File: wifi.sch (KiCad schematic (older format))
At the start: 70 parts

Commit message: gpio assignment done
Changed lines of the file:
@@
 $Descr A4 11693 8268
 encoding utf-8
-Sheet 9 10
+Sheet 8 10
 Title ""
 Date ""
@@
 $EndComp
 Wire Wire Line
-	2950 3825 2950 3925
+	2950 3825 2950 3875
+Wire Wire Line
+	2950 3875 2950 3925
 Wire Wire Line
 	2950 3925 3000 3925
@@
 $EndComp
 Wire Wire Line
-	4300 3825 4300 3925
+	4300 3825 4300 3875
+Wire Wire Line
+	4300 3875 4300 3925
 Wire Wire Line
 	4300 3925 4200 3925
@@
 	1200 4825 2025 4825
 Wire Wire Line
-	2325 4825 3000 4825
+	2325 4825 2425 4825
+Wire Wire Line
+	2425 4825 3000 4825
 Wire Wire Line
 	2425 4875 2425 4825
@@
 	1100 4525 3000 4525
 Wire Wire Line
-	1100 3425 1100 3625
-Wire Wire Line
-	1100 3475 1725 3475
+	1100 3425 1100 3475
+Wire Wire Line
+	1100 3475 1100 3625
+Wire Wire Line
+	1100 3475 1225 3475
+Wire Wire Line
+	1225 3475 1350 3475
+Wire Wire Line
+	1350 3475 1475 3475
+Wire Wire Line
+	1475 3475 1600 3475
+Wire Wire Line
+	1600 3475 1725 3475
 Wire Wire Line
 	1725 3475 1725 3625
@@
 $EndComp
 Wire Wire Line
-	6925 1900 6925 3600
+	6925 1900 6925 2500
+Wire Wire Line
+	6925 2500 6925 2700
+Wire Wire Line
+	6925 2700 6925 3300
+Wire Wire Line
+	6925 3300 6925 3400
+Wire Wire Line
+	6925 3400 6925 3500
+Wire Wire Line
+	6925 3500 6925 3600
 Wire Wire Line
 	6925 1900 7025 1900
@@
 	6825 3100 7025 3100
 Wire Wire Line
-	6825 3200 7025 3200
+	6825 3200 6875 3200
+Wire Wire Line
+	6875 3200 7025 3200
 Text Label 5950 2800 0    60   ~ 0
 WL_SDIO_D0
@@
 $EndComp
 Wire Wire Line
-	2950 5550 2950 5650
+	2950 5550 2950 5600
+Wire Wire Line
+	2950 5600 2950 5650
 Wire Wire Line
 	2950 5650 3000 5650
@@
 $EndComp
 Wire Wire Line
-	4300 5550 4300 5650
+	4300 5550 4300 5600
+Wire Wire Line
+	4300 5600 4300 5650
 Wire Wire Line
 	4300 5650 4200 5650
@@
 	2400 6600 2400 5950
 Wire Wire Line
-	1600 5950 3000 5950
-Wire Wire Line
-	1600 5850 3000 5850
+	1600 5950 2400 5950
+Wire Wire Line
+	2400 5950 3000 5950
+Wire Wire Line
+	1600 5850 2200 5850
+Wire Wire Line
+	2200 5850 3000 5850
 Wire Wire Line
 	2200 5850 2200 6600
@@
 	4400 6600 4400 6350
 Wire Wire Line
-	4200 6350 5750 6350
+	4200 6350 4400 6350
+Wire Wire Line
+	4400 6350 5750 6350
 Wire Wire Line
 	4600 6600 4600 6150
 Wire Wire Line
-	4200 6150 5750 6150
+	4200 6150 4600 6150
+Wire Wire Line
+	4600 6150 5750 6150
 Wire Wire Line
 	4200 5750 5750 5750
@@
 $EndComp
 Wire Wire Line
-	7925 3900 7925 4000
+	7925 3900 7925 3975
+Wire Wire Line
+	7925 3975 7925 4000
 Wire Wire Line
 	8025 3900 8025 3975
 Wire Wire Line
-	7925 3975 9125 3975
+	7925 3975 8025 3975
+Wire Wire Line
+	8025 3975 8325 3975
+Wire Wire Line
+	8325 3975 8425 3975
+Wire Wire Line
+	8425 3975 8825 3975
+Wire Wire Line
+	8825 3975 8925 3975
+Wire Wire Line
+	8925 3975 9025 3975
+Wire Wire Line
+	9025 3975 9125 3975
 Connection ~ 7925 3975
 Wire Wire Line
@@
 $EndComp
 Wire Wire Line
-	9225 3900 9225 4425
+	9225 3900 9225 4400
+Wire Wire Line
+	9225 4400 9225 4425
 $Comp
 L CONN_COAXIAL J?
@@
 	8725 4050 8725 3900
 Wire Wire Line
-	10125 1900 10125 3600
+	10125 1900 10125 2000
+Wire Wire Line
+	10125 2000 10125 2300
+Wire Wire Line
+	10125 2300 10125 2400
+Wire Wire Line
+	10125 2400 10125 2900
+Wire Wire Line
+	10125 2900 10125 3100
+Wire Wire Line
+	10125 3100 10125 3300
+Wire Wire Line
+	10125 3300 10125 3400
+Wire Wire Line
+	10125 3400 10125 3500
+Wire Wire Line
+	10125 3500 10125 3600
 Wire Wire Line
 	10125 1900 10025 1900
@@
 $EndComp
 Wire Wire Line
-	6425 5400 6900 5400
-Wire Wire Line
-	6850 5350 6850 5450
+	6425 5400 6850 5400
+Wire Wire Line
+	6850 5400 6900 5400
+Wire Wire Line
+	6850 5350 6850 5400
+Wire Wire Line
+	6850 5400 6850 5450
 Connection ~ 6850 5400
 $Comp
@@
 	10025 2500 10150 2500
 Wire Wire Line
-	10025 2100 10975 2100
+	10025 2100 10200 2100
+Wire Wire Line
+	10200 2100 10750 2100
+Wire Wire Line
+	10750 2100 10850 2100
+Wire Wire Line
+	10850 2100 10975 2100
 Wire Wire Line
 	10200 2100 10200 2200
@@
 	10850 3000 10850 2950
 Wire Wire Line
-	10025 3000 11000 3000
+	10025 3000 10750 3000
+Wire Wire Line
+	10750 3000 10850 3000
+Wire Wire Line
+	10850 3000 11000 3000
 $Comp
 L C C?
@@
 $EndComp
 Wire Wire Line
-	7750 1400 8825 1400
+	7750 1400 7825 1400
+Wire Wire Line
+	7825 1400 7925 1400
+Wire Wire Line
+	7925 1400 8125 1400
+Wire Wire Line
+	8125 1400 8325 1400
+Wire Wire Line
+	8325 1400 8725 1400
+Wire Wire Line
+	8725 1400 8825 1400
 Wire Wire Line
 	8825 1400 8825 1450

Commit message: gpio connectors
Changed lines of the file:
@@
 $EndComp
 Wire Wire Line
-	2950 3825 2950 3875
-Wire Wire Line
-	2950 3875 2950 3925
+	2950 3825 2950 3925
 Wire Wire Line
 	2950 3925 3000 3925
@@
 $EndComp
 Wire Wire Line
-	4300 3825 4300 3875
-Wire Wire Line
-	4300 3875 4300 3925
+	4300 3825 4300 3925
 Wire Wire Line
 	4300 3925 4200 3925
@@
 	1200 4825 2025 4825
 Wire Wire Line
-	2325 4825 2425 4825
-Wire Wire Line
-	2425 4825 3000 4825
+	2325 4825 3000 4825
 Wire Wire Line
 	2425 4875 2425 4825
@@
 	1100 4525 3000 4525
 Wire Wire Line
-	1100 3425 1100 3475
-Wire Wire Line
-	1100 3475 1100 3625
-Wire Wire Line
-	1100 3475 1225 3475
-Wire Wire Line
-	1225 3475 1350 3475
-Wire Wire Line
-	1350 3475 1475 3475
-Wire Wire Line
-	1475 3475 1600 3475
-Wire Wire Line
-	1600 3475 1725 3475
+	1100 3425 1100 3625
+Wire Wire Line
+	1100 3475 1725 3475
 Wire Wire Line
 	1725 3475 1725 3625
@@
 $EndComp
 Wire Wire Line
-	6925 1900 6925 2500
-Wire Wire Line
-	6925 2500 6925 2700
-Wire Wire Line
-	6925 2700 6925 3300
-Wire Wire Line
-	6925 3300 6925 3400
-Wire Wire Line
-	6925 3400 6925 3500
-Wire Wire Line
-	6925 3500 6925 3600
+	6925 1900 6925 3600
 Wire Wire Line
 	6925 1900 7025 1900
@@
 	6825 3100 7025 3100
 Wire Wire Line
-	6825 3200 6875 3200
-Wire Wire Line
-	6875 3200 7025 3200
+	6825 3200 7025 3200
 Text Label 5950 2800 0    60   ~ 0
 WL_SDIO_D0
@@
 $EndComp
 Wire Wire Line
-	2950 5550 2950 5600
-Wire Wire Line
-	2950 5600 2950 5650
+	2950 5550 2950 5650
 Wire Wire Line
 	2950 5650 3000 5650
@@
 $EndComp
 Wire Wire Line
-	4300 5550 4300 5600
-Wire Wire Line
-	4300 5600 4300 5650
+	4300 5550 4300 5650
 Wire Wire Line
 	4300 5650 4200 5650
@@
 	2400 6600 2400 5950
 Wire Wire Line
-	1600 5950 2400 5950
-Wire Wire Line
-	2400 5950 3000 5950
-Wire Wire Line
-	1600 5850 2200 5850
-Wire Wire Line
-	2200 5850 3000 5850
+	1600 5950 3000 5950
+Wire Wire Line
+	1600 5850 3000 5850
 Wire Wire Line
 	2200 5850 2200 6600
@@
 	4400 6600 4400 6350
 Wire Wire Line
-	4200 6350 4400 6350
-Wire Wire Line
-	4400 6350 5750 6350
+	4200 6350 5750 6350
 Wire Wire Line
 	4600 6600 4600 6150
 Wire Wire Line
-	4200 6150 4600 6150
-Wire Wire Line
-	4600 6150 5750 6150
+	4200 6150 5750 6150
 Wire Wire Line
 	4200 5750 5750 5750
@@
 $EndComp
 Wire Wire Line
-	7925 3900 7925 3975
-Wire Wire Line
-	7925 3975 7925 4000
+	7925 3900 7925 4000
 Wire Wire Line
 	8025 3900 8025 3975
 Wire Wire Line
-	7925 3975 8025 3975
-Wire Wire Line
-	8025 3975 8325 3975
-Wire Wire Line
-	8325 3975 8425 3975
-Wire Wire Line
-	8425 3975 8825 3975
-Wire Wire Line
-	8825 3975 8925 3975
-Wire Wire Line
-	8925 3975 9025 3975
-Wire Wire Line
-	9025 3975 9125 3975
+	7925 3975 9125 3975
 Connection ~ 7925 3975
 Wire Wire Line
@@
 $EndComp
 Wire Wire Line
-	9225 3900 9225 4400
-Wire Wire Line
-	9225 4400 9225 4425
+	9225 3900 9225 4425
 $Comp
 L CONN_COAXIAL J?
@@
 	8725 4050 8725 3900
 Wire Wire Line
-	10125 1900 10125 2000
-Wire Wire Line
-	10125 2000 10125 2300
-Wire Wire Line
-	10125 2300 10125 2400
-Wire Wire Line
-	10125 2400 10125 2900
-Wire Wire Line
-	10125 2900 10125 3100
-Wire Wire Line
-	10125 3100 10125 3300
-Wire Wire Line
-	10125 3300 10125 3400
-Wire Wire Line
-	10125 3400 10125 3500
-Wire Wire Line
-	10125 3500 10125 3600
+	10125 1900 10125 3600
 Wire Wire Line
 	10125 1900 10025 1900
@@
 $EndComp
 Wire Wire Line
-	6425 5400 6850 5400
-Wire Wire Line
-	6850 5400 6900 5400
-Wire Wire Line
-	6850 5350 6850 5400
-Wire Wire Line
-	6850 5400 6850 5450
+	6425 5400 6900 5400
+Wire Wire Line
+	6850 5350 6850 5450
 Connection ~ 6850 5400
 $Comp
@@
 	10025 2500 10150 2500
 Wire Wire Line
-	10025 2100 10200 2100
-Wire Wire Line
-	10200 2100 10750 2100
-Wire Wire Line
-	10750 2100 10850 2100
-Wire Wire Line
-	10850 2100 10975 2100
+	10025 2100 10975 2100
 Wire Wire Line
 	10200 2100 10200 2200
@@
 	10850 3000 10850 2950
 Wire Wire Line
-	10025 3000 10750 3000
-Wire Wire Line
-	10750 3000 10850 3000
-Wire Wire Line
-	10850 3000 11000 3000
+	10025 3000 11000 3000
 $Comp
 L C C?
@@
 $EndComp
 Wire Wire Line
-	7750 1400 7825 1400
-Wire Wire Line
-	7825 1400 7925 1400
-Wire Wire Line
-	7925 1400 8125 1400
-Wire Wire Line
-	8125 1400 8325 1400
-Wire Wire Line
-	8325 1400 8725 1400
-Wire Wire Line
-	8725 1400 8825 1400
+	7750 1400 8825 1400
 Wire Wire Line
 	8825 1400 8825 1450

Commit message: annotation, wip erc
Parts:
- gave numbers to parts that had none: 70

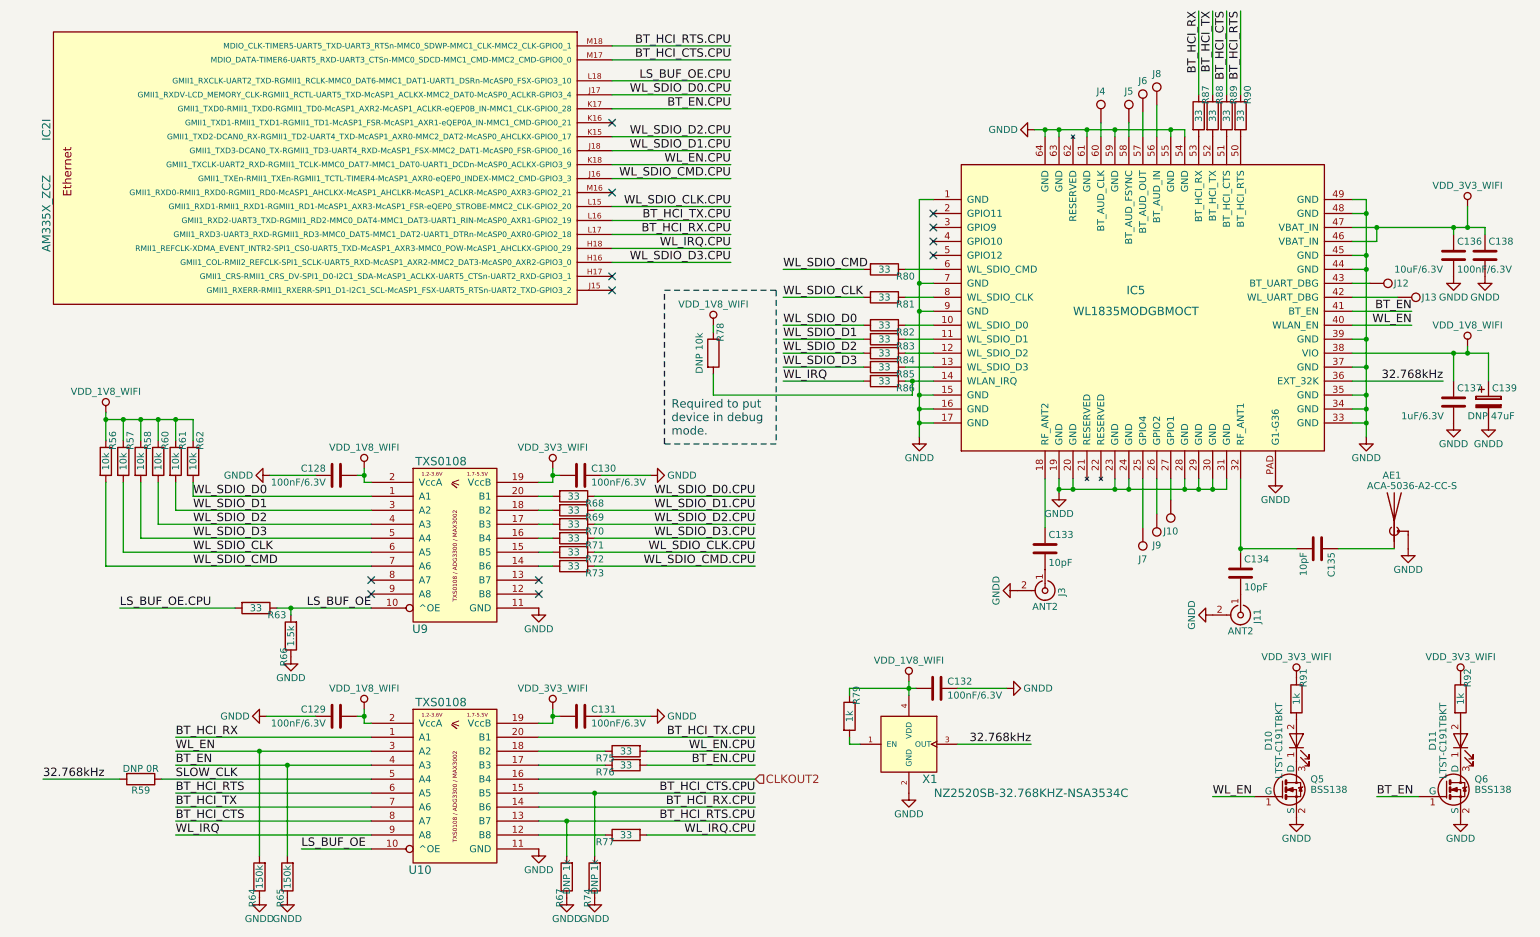
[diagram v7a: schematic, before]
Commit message: only io connectors remaining
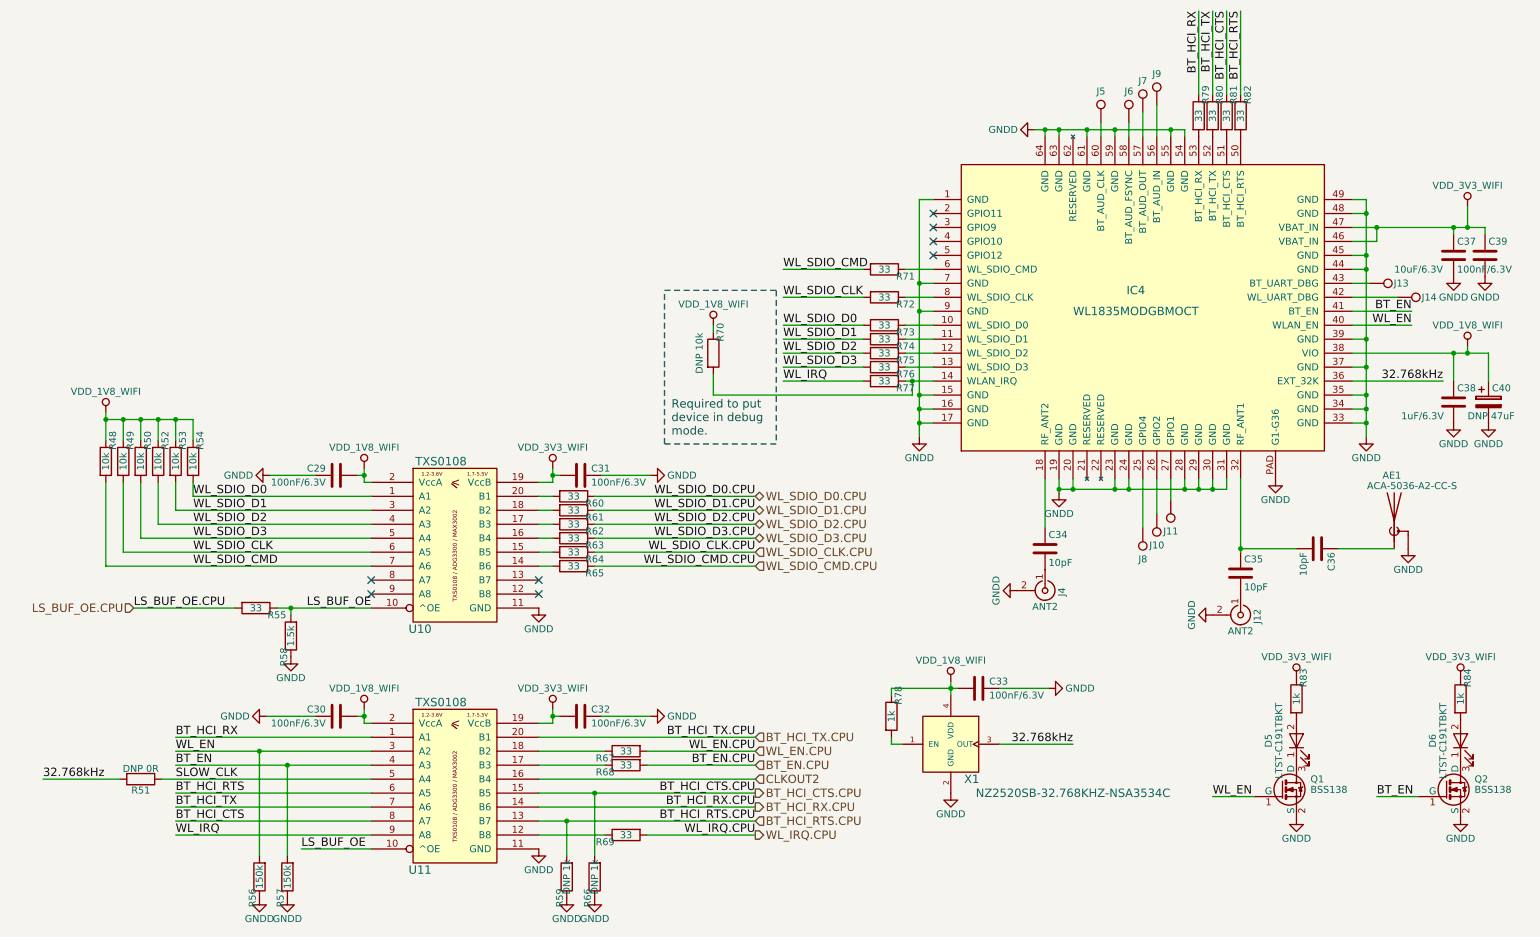
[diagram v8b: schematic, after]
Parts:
- removed IC2: AM335X_ZCZ, symbol AM335X_ZCZ
- renumbered C128 to C29, C129 to C30, C130 to C31, C131 to C32, C132 to C33, C133 to C34, C134 to C35, C135 to C36, C136 to C37, C137 to C38, C138 to C39, C139 to C40, D10 to D5, D11 to D6, IC5 to IC4, J9 to J10, J10 to J11, J11 to J12, J12 to J13, J13 to J14, J3 to J4, J4 to J5, J5 to J6, J6 to J7, J7 to J8, J8 to J9, Q5 to Q1, Q6 to Q2, R56 to R48, R57 to R49, R58 to R50, R59 to R51, R60 to R52, R61 to R53, R62 to R54, R63 to R55, R64 to R56, R65 to R57, R66 to R58, R67 to R59, R68 to R60, R69 to R61, R70 to R62, R71 to R63, R72 to R64, R73 to R65, R74 to R66, R75 to R67, R76 to R68, R77 to R69, R78 to R70, R80 to R71, R81 to R72, R82 to R73, R83 to R74, R84 to R75, R85 to R76, R86 to R77, R79 to R78, R87 to R79, R88 to R80, R89 to R81, R90 to R82, R91 to R83, R92 to R84, U9 to U10, U10 to U11
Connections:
- no-connect marks 12 -> 8
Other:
- moved on the sheet: C33, R78, X1
